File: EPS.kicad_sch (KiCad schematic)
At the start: 36 parts, among them SW101 Deploy, SW102 Deploy

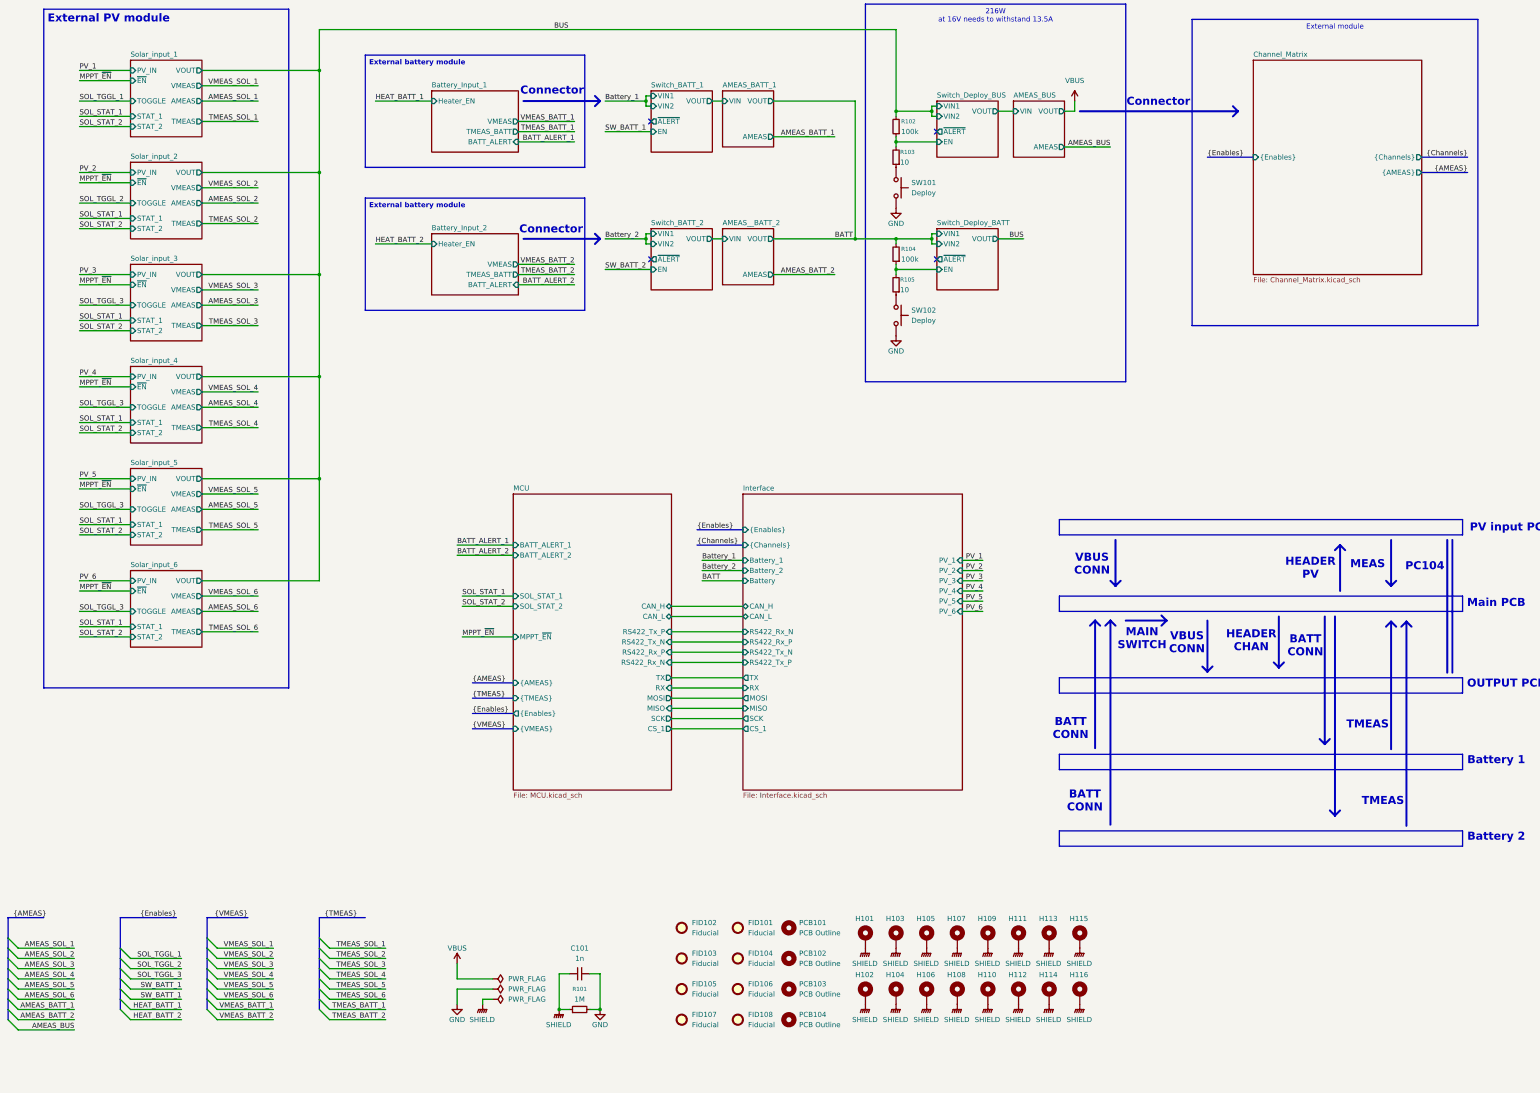
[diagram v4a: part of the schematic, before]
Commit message: wired channel alerts; added schematic for test pbc
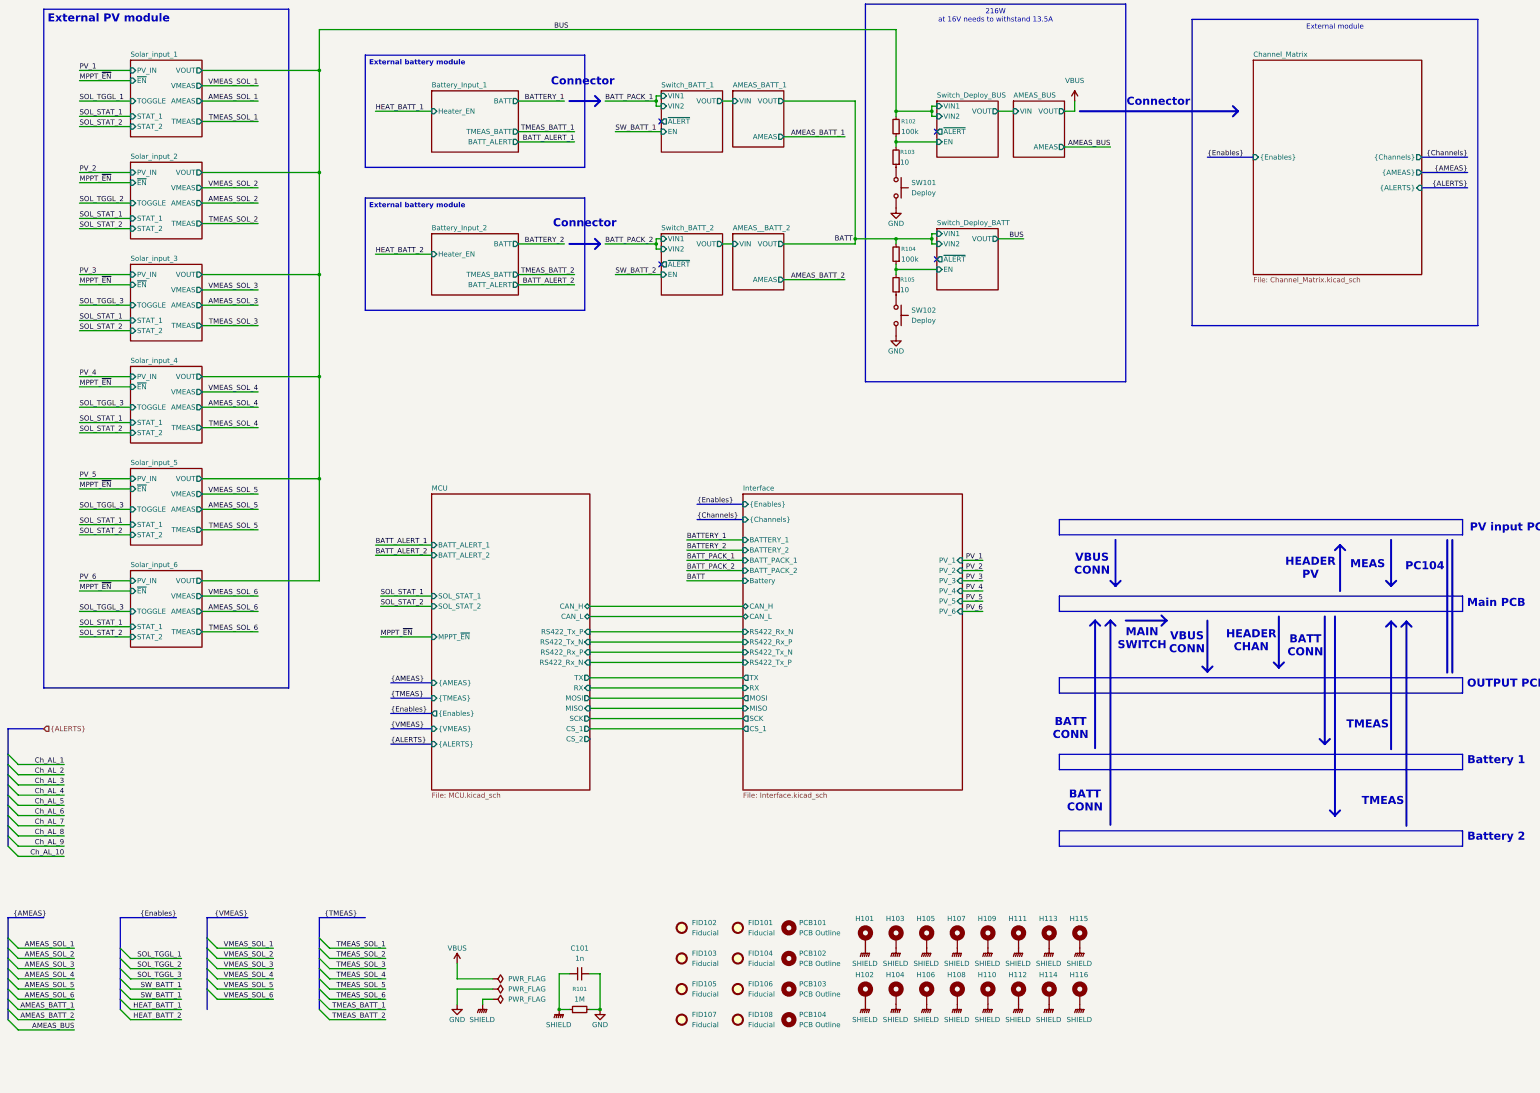
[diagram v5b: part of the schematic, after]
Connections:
- net BATT: no longer R104.2
- new net AMEAS_BATT_1/VOUT: R104.2
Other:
- sheet Battery_Input_1 ports: added BATT; removed VMEAS
- sheet Battery_Input_2 ports: added BATT; removed VMEAS
- sheet Channel_Matrix ports: added {ALERTS}; removed none
- sheet Interface ports: added BATTERY_1, BATTERY_2, BATT_PACK_1, BATT_PACK_2; removed Battery_1, Battery_2
- sheet MCU ports: added CS_2, {ALERTS}; removed none

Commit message: reduced number of DCDC converter for PV panels; updated test pcb
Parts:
- added D101, D102, D103, D104, D105, D106: D_Schottky, Diode_SMD:D_0805_2012Metric, symbol Device:D_Schottky
- R102, R104: value 100k -> 1M
- R103, R105: value 10 -> TBD
- renumbered FID102 to FID101, FID103 to FID102, FID105 to FID103, FID107 to FID104, FID101 to FID105, FID104 to FID106, FID106 to FID107
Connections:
- net AMEAS_BATT_1/VOUT is gone; now on net BATT: R104.2
- net GND: now also R103.1, R105.1
- net PV_1: now also D101.2 (A)
- net PV_2: now also D102.2 (A)
- net PV_3: now also D103.2 (A)
- net PV_4: now also D104.2 (A)
- net PV_5: now also D105.2 (A)
- net PV_6: now also D106.2 (A)
- net Switch_Deploy_BATT/EN: now also SW102.1
- net Switch_Deploy_BUS/EN: now also SW101.1
- new net 5V_DCDC_1/EN: D101.1 (K), D102.1 (K), D103.1 (K), D104.1 (K), D105.1 (K), D106.1 (K)
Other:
- added sheet 5V_DCDC_1 (DCDC_ADJUCTABLE.kicad_sch)
- sheet Solar_input_1 ports: added FIXED_IN; removed none
- sheet Solar_input_2 ports: added FIXED_IN; removed none
- sheet Solar_input_3 ports: added FIXED_IN; removed none
- sheet Solar_input_4 ports: added FIXED_IN; removed none
- sheet Solar_input_5 ports: added FIXED_IN; removed none
- sheet Solar_input_6 ports: added FIXED_IN; removed none
- note added: "Shared backup DCDC to save space"
- moved on the sheet: R102, R103, R104, R105, SW101, SW102

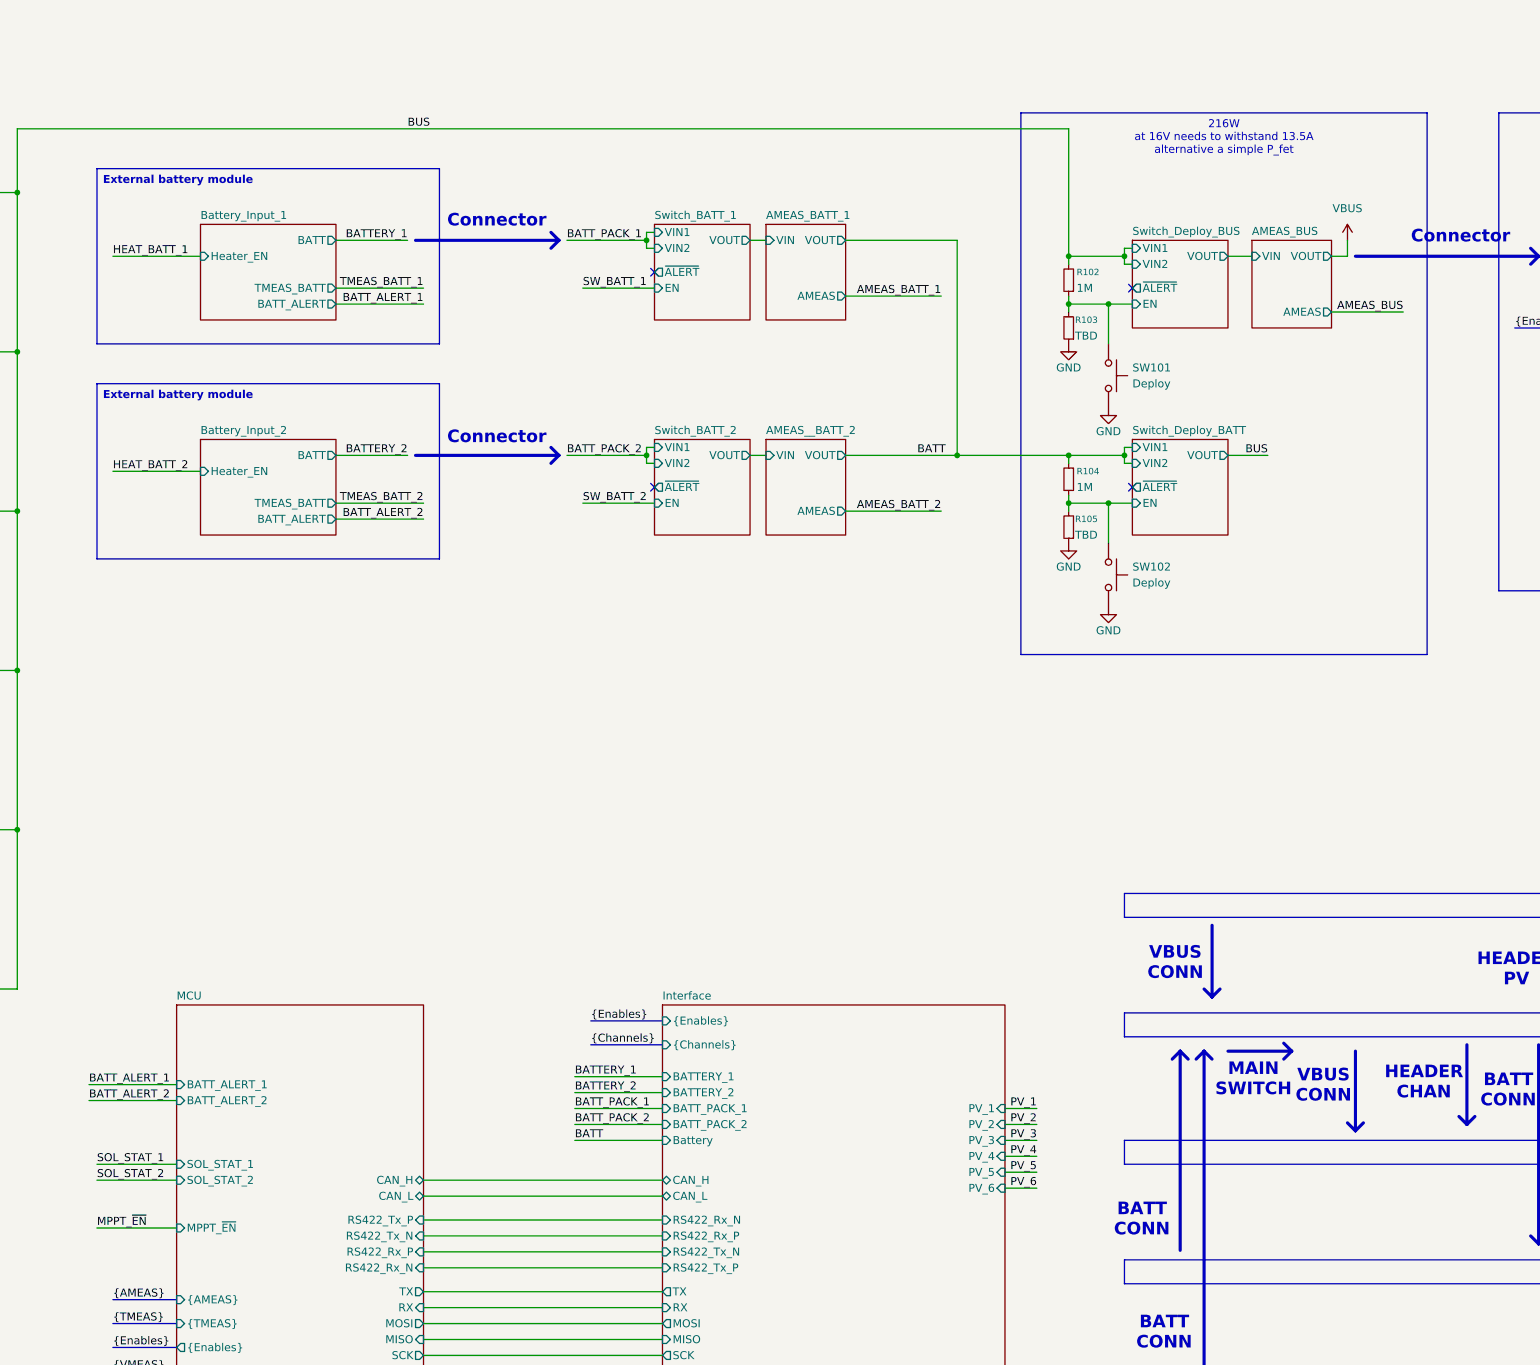
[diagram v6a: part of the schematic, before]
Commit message: added missing heater connectors
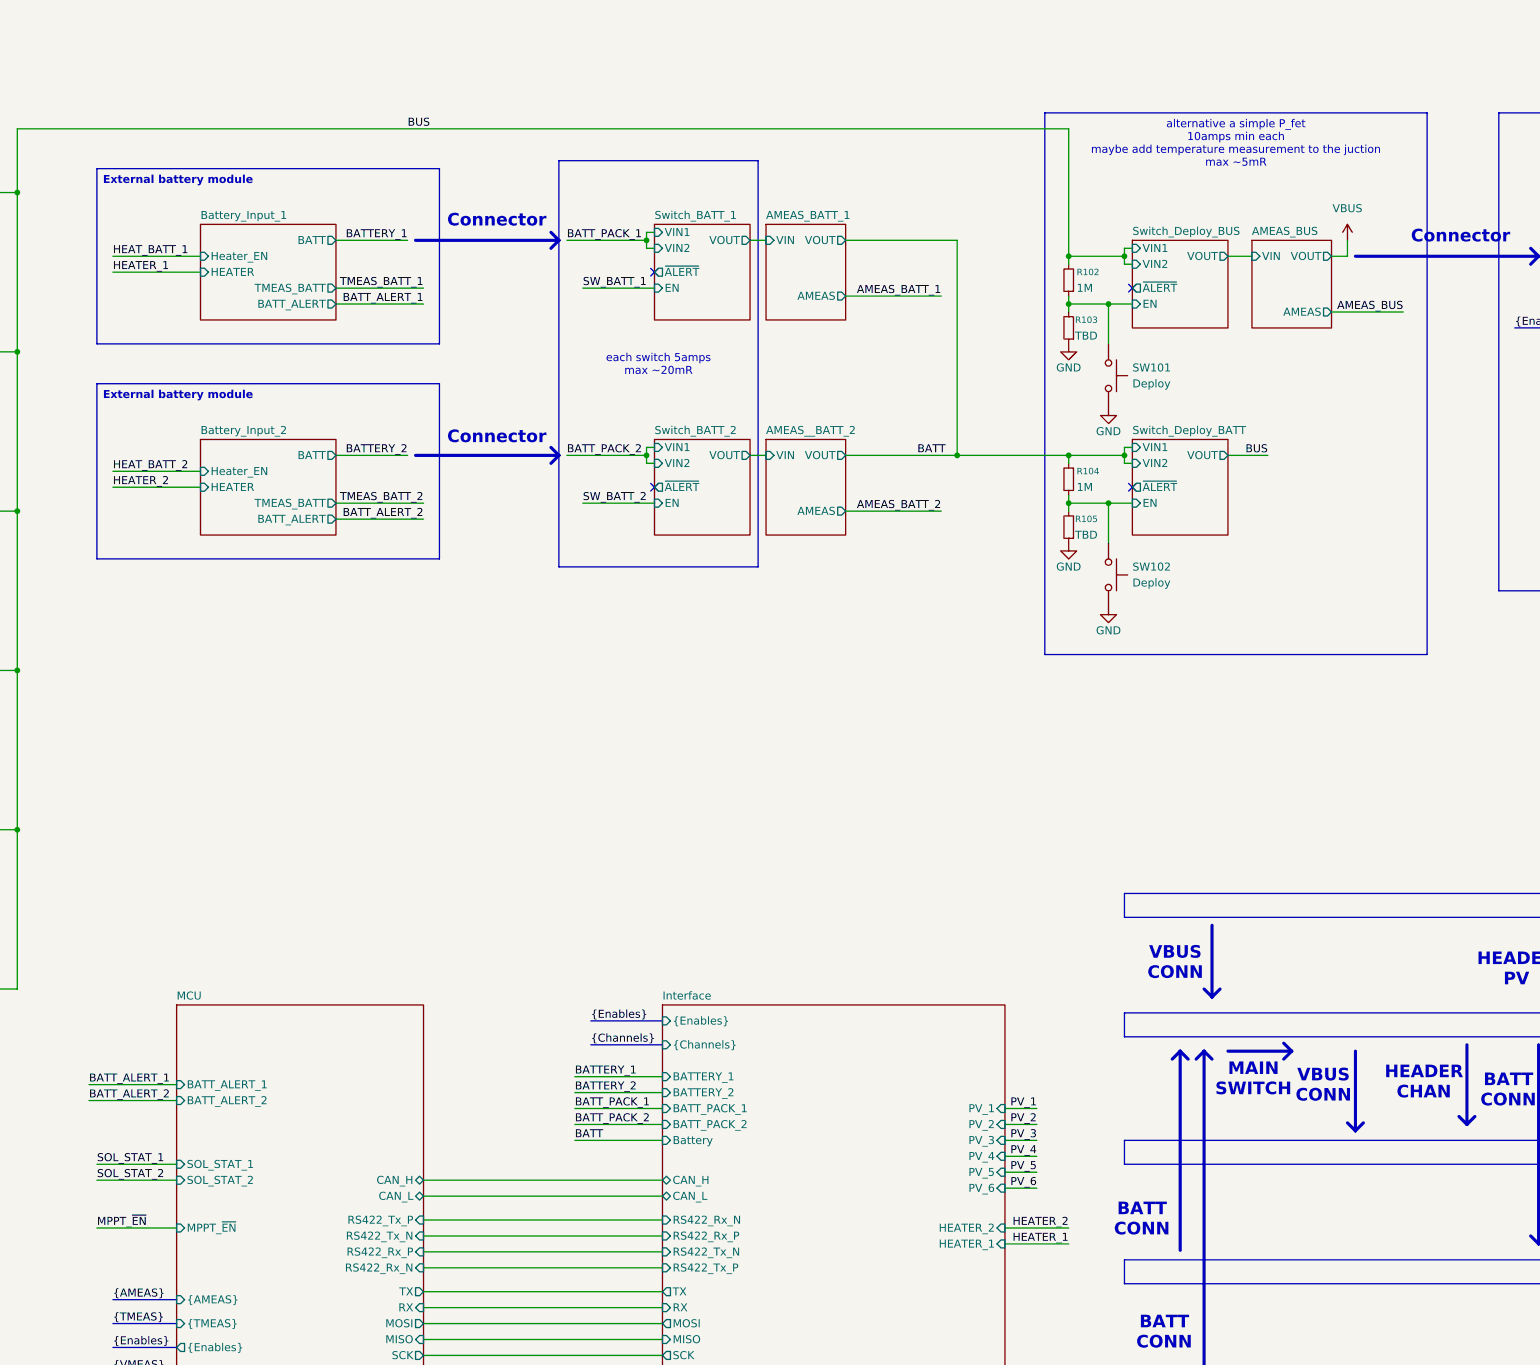
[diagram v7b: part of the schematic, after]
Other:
- sheet Battery_Input_1 ports: added HEATER; removed none
- sheet Battery_Input_2 ports: added HEATER; removed none
- sheet Interface ports: added HEATER_1, HEATER_2; removed none
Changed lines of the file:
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@@
 		)
 	)
+	(text_box "each switch 5amps\nmax ~20mR"
+		(exclude_from_sim no)
+		(at 194.31 35.56 0)
+		(size 31.75 64.77)
+		(margins 0.9525 0.9525 0.9525 0.9525)
+		(stroke
+			(width 0)
+			(type solid)
+		)
+		(fill
+			(type none)
+		)
+		(effects
+			(font
+				(size 1.27 1.27)
+			)
+		)
+	)
 	(text_box "External module"
 		(exclude_from_sim no)
@@
 		)
 	)
-	(text_box "216W\nat 16V needs to withstand 13.5A\nalternative a simple P_fet"
+	(text_box "alternative a simple P_fet\n10amps min each\nmaybe add temperature measurement to the juction\nmax ~5mR"
 		(exclude_from_sim no)
-		(at 267.97 27.94 0)
-		(size 64.77 86.36)
+		(at 271.78 27.94 0)
+		(size 60.96 86.36)
 		(margins 0.9525 0.9525 0.9525 0.9525)
 		(stroke
@@
 	(wire
 		(pts
+			(xy 265.43 208.28) (xy 275.59 208.28)
+		)
+		(stroke
+			(width 0)
+			(type default)
+		)
+	)
+	(wire
+		(pts
 			(xy 35.56 212.09) (xy 45.72 212.09)
 		)
@@
 	(wire
 		(pts
+			(xy 265.43 205.74) (xy 275.59 205.74)
+		)
+		(stroke
+			(width 0)
+			(type default)
+		)
+	)
+	(wire
+		(pts
 			(xy 71.12 95.25) (xy 85.09 95.25)
 		)
@@
 	(wire
 		(pts
+			(xy 123.19 87.63) (xy 137.16 87.63)
+		)
+		(stroke
+			(width 0)
+			(type default)
+		)
+	)
+	(wire
+		(pts
 			(xy 107.95 116.84) (xy 107.95 91.44)
 		)
@@
 	(wire
 		(pts
+			(xy 123.19 53.34) (xy 137.16 53.34)
+		)
+		(stroke
+			(width 0)
+			(type default)
+		)
+	)
+	(wire
+		(pts
 			(xy 55.88 227.33) (xy 55.88 232.41)
 		)
@@
 		)
 	)
+	(label "HEATER_1"
+		(at 275.59 208.28 180)
+		(effects
+			(font
+				(size 1.27 1.27)
+			)
+			(justify right bottom)
+		)
+	)
 	(label "SOL_STAT_2"
 		(at 120.65 198.12 0)
@@
 		)
 	)
+	(label "HEATER_2"
+		(at 123.19 87.63 0)
+		(effects
+			(font
+				(size 1.27 1.27)
+			)
+			(justify left bottom)
+		)
+	)
 	(label "SOL_STAT_2"
 		(at 40.64 156.21 0)
@@
 		)
 	)
+	(label "HEATER_2"
+		(at 275.59 205.74 180)
+		(effects
+			(font
+				(size 1.27 1.27)
+			)
+			(justify right bottom)
+		)
+	)
 	(label "AMEAS_BUS"
 		(at 328.93 59.69 180)
@@
 		)
 	)
+	(label "HEATER_1"
+		(at 123.19 53.34 0)
+		(effects
+			(font
+				(size 1.27 1.27)
+			)
+			(justify left bottom)
+		)
+	)
 	(label "AMEAS_SOL_1"
 		(at 62.23 257.81 180)
@@
 			)
 		)
+		(pin "HEATER" input
+			(at 137.16 53.34 180)
+			(effects
+				(font
+					(size 1.27 1.27)
+				)
+				(justify left)
+			)
+		)
 		(instances
 			(project "EPS"
@@
 			)
 		)
+		(pin "HEATER_1" input
+			(at 265.43 208.28 0)
+			(effects
+				(font
+					(size 1.27 1.27)
+				)
+				(justify right)
+			)
+		)
+		(pin "HEATER_2" input
+			(at 265.43 205.74 0)
+			(effects
+				(font
+					(size 1.27 1.27)
+				)
+				(justify right)
+			)
+		)
 		(instances
 			(project "EPS"
@@
 			)
 		)
+		(pin "HEATER" input
+			(at 137.16 87.63 180)
+			(effects
+				(font
+					(size 1.27 1.27)
+				)
+				(justify left)
+			)
+		)
